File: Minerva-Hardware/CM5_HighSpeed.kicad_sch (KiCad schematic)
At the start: 13 parts, among them J16 Conn_01x22_Female, J5 Conn_01x22_Female, J6 THD-02-R, U6 AP22653W6

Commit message: Rename and commit actions due to mishap of location naming/saving
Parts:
- added J1: HDMI_D_1.4, Connector_Video:HDMI_A_Kycon_KDMIX-SL1-NS-WS-B15_VerticalRightAngle, symbol Connector:HDMI_D_1.4
- U6: Field5 31-AP22653W6-7CT-ND -> AP2553W6-7DICT-ND
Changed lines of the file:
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@@
 			)
 		)
-		(property "Datasheet" "https://fscdn.rohm.com/en/products/databook/datasheet/passive/resistor/chip_resistor/mcr-e.pdf"
+		(property "Datasheet" "~"
 			(at 207.01 110.49 0)
 			(effects
@@
 			)
 		)
-		(property "Description" ""
+		(property "Description" "Resistor"
 			(at 207.01 110.49 0)
 			(effects
@@
 			)
 		)
-		(property "Datasheet" "https://fscdn.rohm.com/en/products/databook/datasheet/passive/resistor/chip_resistor/mcr-e.pdf"
+		(property "Datasheet" "~"
 			(at 214.63 110.49 0)
 			(effects
@@
 			)
 		)
-		(property "Description" ""
+		(property "Description" "Resistor"
 			(at 214.63 110.49 0)
 			(effects
@@
 			)
 		)
-		(property "Datasheet" "https://www.hirose.com/product/document?clcode=&productname=&series=FH12&documenttype=Catalog&lang=en&documentid=D31648_en"
+		(property "Datasheet" "~"
 			(at 156.21 50.8 0)
 			(effects
@@
 			)
 		)
-		(property "Description" ""
+		(property "Description" "Generic connector, single row, 01x22, script generated"
 			(at 156.21 50.8 0)
 			(effects
@@
 			)
 		)
-		(property "Datasheet" "https://www.hirose.com/product/document?clcode=&productname=&series=FH12&documenttype=Catalog&lang=en&documentid=D31648_en"
+		(property "Datasheet" "~"
 			(at 156.21 121.92 0)
 			(effects
@@
 			)
 		)
-		(property "Description" ""
+		(property "Description" "Generic connector, single row, 01x22, script generated"
 			(at 156.21 121.92 0)
 			(effects
@@
 			)
 		)
-		(property "Datasheet" "https://www.toby.co.uk/uploads/publications/1673.pdf"
+		(property "Datasheet" "~"
 			(at 196.85 119.38 0)
 			(effects
@@
 			)
 		)
-		(property "Description" ""
+		(property "Description" "Generic connector, double row, 02x02, odd/even pin numbering scheme (row 1 odd numbers, row 2 even numbers), script generated (kicad-library-utils/schlib/autogen/connector/)"
 			(at 196.85 119.38 0)
 			(effects
@@
 				(path "/e63e39d7-6ac0-4ffd-8aa3-1841a4541b55/00000000-0000-0000-0000-00005cff70b1"
 					(reference "J6")
+					(unit 1)
+				)
+			)
+		)
+	)
+	(symbol
+		(lib_id "Connector:HDMI_D_1.4")
+		(at 223.52 46.99 0)
+		(unit 1)
+		(exclude_from_sim no)
+		(in_bom yes)
+		(on_board yes)
+		(dnp no)
+		(fields_autoplaced yes)
+		(property "Reference" "J1"
+			(at 234.95 45.7199 0)
+			(effects
+				(font
+					(size 1.27 1.27)
+				)
+				(justify left)
+			)
+		)
+		(property "Value" "HDMI_D_1.4"
+			(at 234.95 48.2599 0)
+			(effects
+				(font
+					(size 1.27 1.27)
+				)
+				(justify left)
+			)
+		)
+		(property "Footprint" "Connector_Video:HDMI_A_Kycon_KDMIX-SL1-NS-WS-B15_VerticalRightAngle"
+			(at 224.155 46.99 0)
+			(effects
+				(font
+					(size 1.27 1.27)
+				)
+				(hide yes)
+			)
+		)
+		(property "Datasheet" "http://pinoutguide.com/PortableDevices/micro_hdmi_type_d_pinout.shtml"
+			(at 224.155 46.99 0)
+			(effects
+				(font
+					(size 1.27 1.27)
+				)
+				(hide yes)
+			)
+		)
+		(property "Description" "HDMI 1.4+ type D connector"
+			(at 223.52 46.99 0)
+			(effects
+				(font
+					(size 1.27 1.27)
+				)
+				(hide yes)
+			)
+		)
+		(pin "12"
+		)
+		(pin "7"
+		)
+		(pin "10"
+		)
+		(pin "19"
+		)
+		(pin "15"
+		)
+		(pin "5"
+		)
+		(pin "18"
+		)
+		(pin "16"
+		)
+		(pin "SH"
+		)
+		(pin "14"
+		)
+		(pin "13"
+		)
+		(pin "1"
+		)
+		(pin "17"
+		)
+		(pin "4"
+		)
+		(pin "2"
+		)
+		(pin "11"
+		)
+		(pin "9"
+		)
+		(pin "6"
+		)
+		(pin "3"
+		)
+		(pin "8"
+		)
+		(instances
+			(project "CM5IO"
+				(path "/e63e39d7-6ac0-4ffd-8aa3-1841a4541b55/00000000-0000-0000-0000-00005cff70b1"
+					(reference "J1")
 					(unit 1)
 				)
@@
 			)
 		)
-		(property "Datasheet" "https://search.murata.co.jp/Ceramy/image/img/A01X/G101/ENG/GRM21BR71A106KA73-01.pdf"
+		(property "Datasheet" "~"
 			(at 100.33 181.61 0)
 			(effects
@@
 			)
 		)
-		(property "Description" ""
+		(property "Description" "Unpolarized capacitor"
 			(at 100.33 181.61 0)
 			(effects
@@
 			)
 		)
-		(property "Datasheet" "https://fscdn.rohm.com/en/products/databook/datasheet/passive/resistor/chip_resistor/mcr-e.pdf"
+		(property "Datasheet" "~"
 			(at 138.43 137.16 0)
 			(effects
@@
 			)
 		)
-		(property "Description" ""
+		(property "Description" "Resistor"
 			(at 138.43 137.16 0)
 			(effects
@@
 			)
 		)
-		(property "Description" ""
+		(property "Description" "Polarized capacitor"
 			(at 87.63 181.61 0)
 			(effects
@@
 			)
 		)
-		(property "Datasheet" "https://fscdn.rohm.com/en/products/databook/datasheet/passive/resistor/chip_resistor/mcr-e.pdf"
+		(property "Datasheet" "~"
 			(at 78.74 177.8 0)
 			(effects
@@
 			)
 		)
-		(property "Description" ""
+		(property "Description" "Resistor"
 			(at 78.74 177.8 0)
 			(effects
@@
 			)
 		)
-		(property "Datasheet" "https://search.murata.co.jp/Ceramy/image/img/A01X/G101/ENG/GRM21BR71A106KA73-01.pdf"
+		(property "Datasheet" "~"
 			(at 110.49 181.61 0)
 			(effects
@@
 			)
 		)
-		(property "Description" ""
+		(property "Description" "Unpolarized capacitor"
 			(at 110.49 181.61 0)
 			(effects
@@
 			)
 		)
-		(property "Field5" "	31-AP22653W6-7CT-ND"
+		(property "Field5" "AP2553W6-7DICT-ND"
 			(at 59.69 177.8 0)
 			(effects
@@
 			)
 		)
-		(property "Datasheet" "https://search.murata.co.jp/Ceramy/image/img/A01X/G101/ENG/GRM21BR71A106KA73-01.pdf"
+		(property "Datasheet" "~"
 			(at 29.21 180.34 0)
 			(effects
@@
 			)
 		)
-		(property "Description" ""
+		(property "Description" "Unpolarized capacitor"
 			(at 29.21 180.34 0)
 			(effects

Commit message: renames
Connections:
- net USBOTG_ID: no longer names the net of Module1.101 (USB_OTG_ID)
- no-connect marks 26 -> 27
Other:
- company: Copyright © 2024 Raspberry Pi Ltd. -> (none)
- title: Compute Module 5 IO Board - CM5 - Highspeed -> Minerva Carrier Board - CM5 - Highspeed
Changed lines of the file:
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@@
 	(paper "A4")
 	(title_block
-		(title "Compute Module 5 IO Board - CM5 - Highspeed")
+		(title "Minerva Carrier Board - CM5 - Highspeed")
+		(date "2026-04-13")
 		(rev "1")
-		(company "Copyright © 2024 Raspberry Pi Ltd.")
-		(comment 1 "www.raspberrypi.com")
 	)
 	(text "Jumpers to be fitted if DPHY1 is used\n"
@@
 	)
 	(no_connect
+		(at 99.06 25.4)
+	)
+	(no_connect
 		(at 67.31 180.34)
 	)
@@
 		)
 	)
-	(wire
-		(pts
-			(xy 105.41 25.4) (xy 99.06 25.4)
-		)
-		(stroke
-			(width 0)
-			(type solid)
-		)
-	)
 	(label "DPHY1_D3_P"
 		(at 21.59 144.78 0)
@@
 		)
 	)
-	(hierarchical_label "USBOTG_ID"
-		(shape input)
-		(at 105.41 25.4 0)
-		(effects
-			(font
-				(size 1.27 1.27)
-			)
-			(justify left)
-		)
-	)

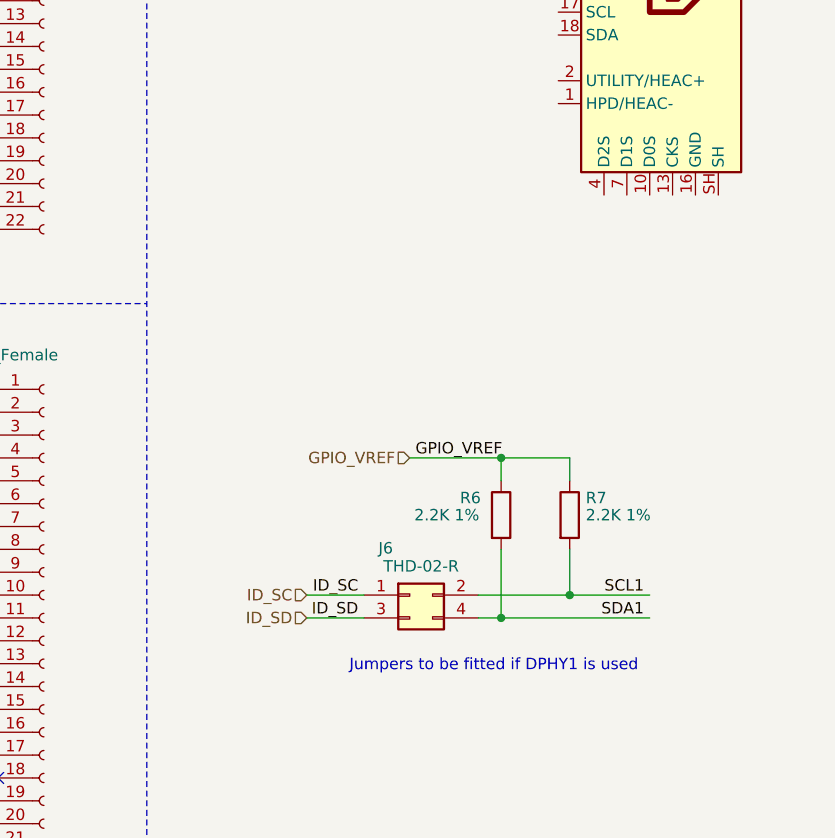
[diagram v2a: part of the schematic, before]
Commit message: Adding MiniPCI-E stuff
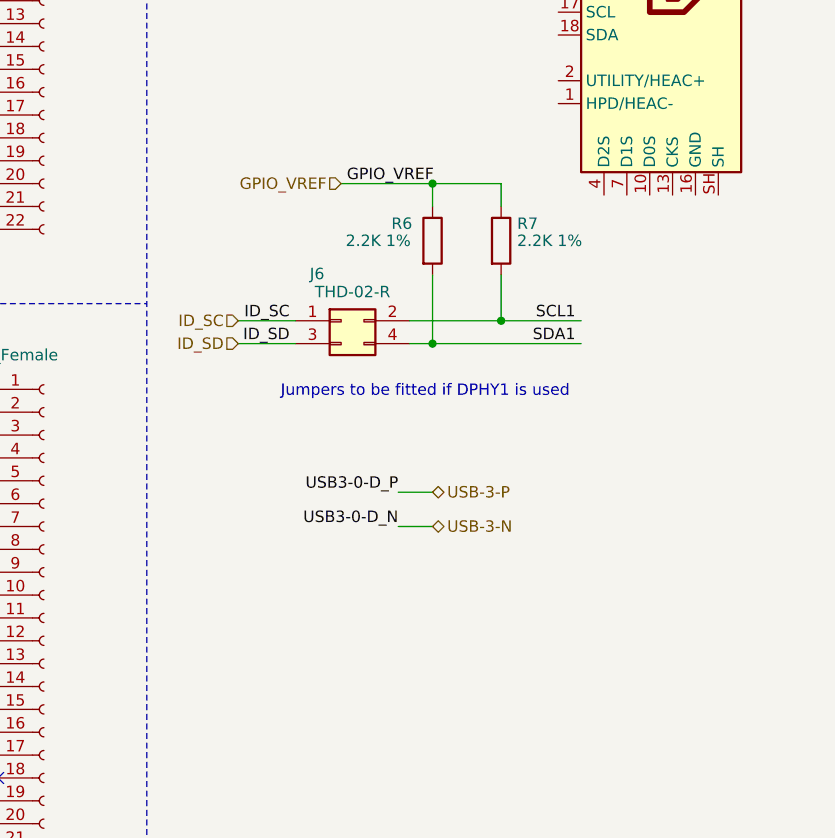
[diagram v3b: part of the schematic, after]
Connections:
- net USB3-0-D_N renamed USB-3-N
- net USB3-0-D_P renamed USB-3-P
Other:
- moved on the sheet: J6, R6, R7

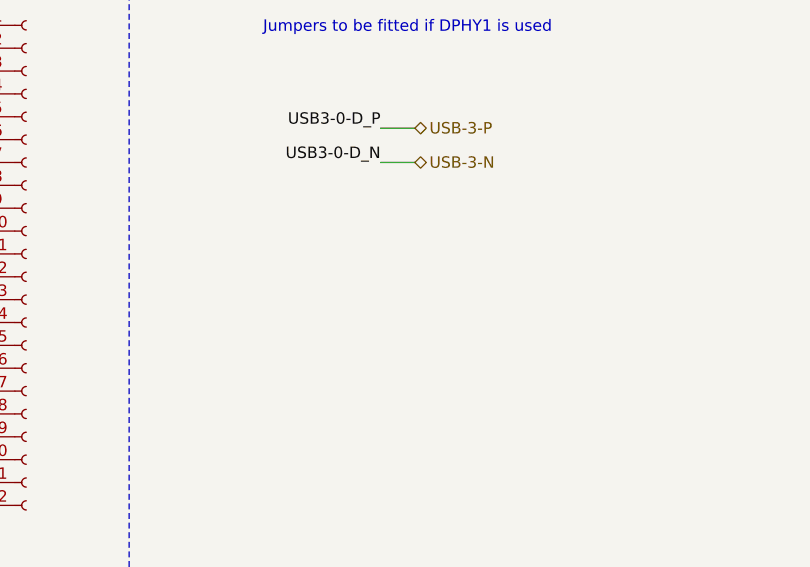
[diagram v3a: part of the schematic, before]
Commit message: Adding in the M.2 B WWAN
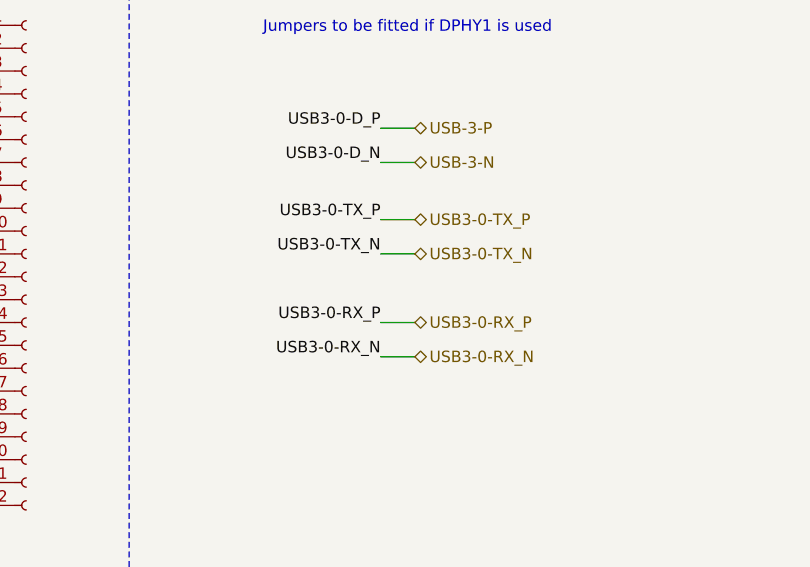
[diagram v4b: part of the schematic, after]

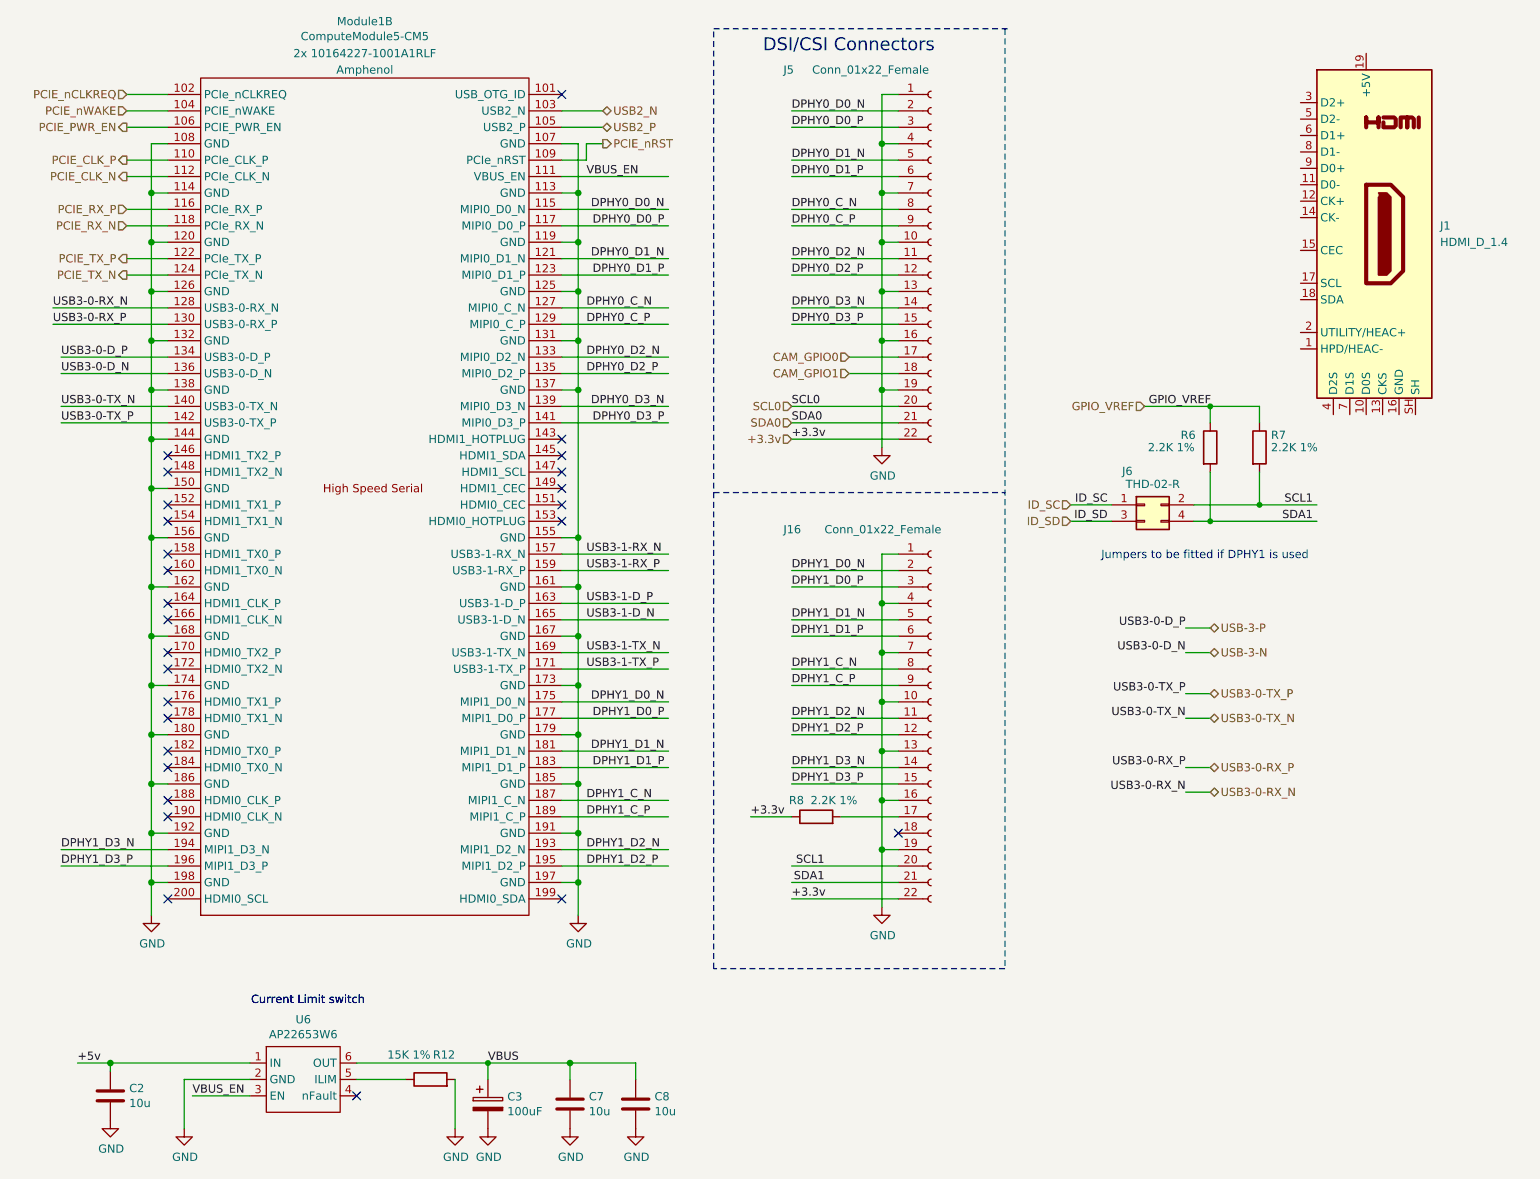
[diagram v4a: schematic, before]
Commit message: Redid the BQ powerpath unit
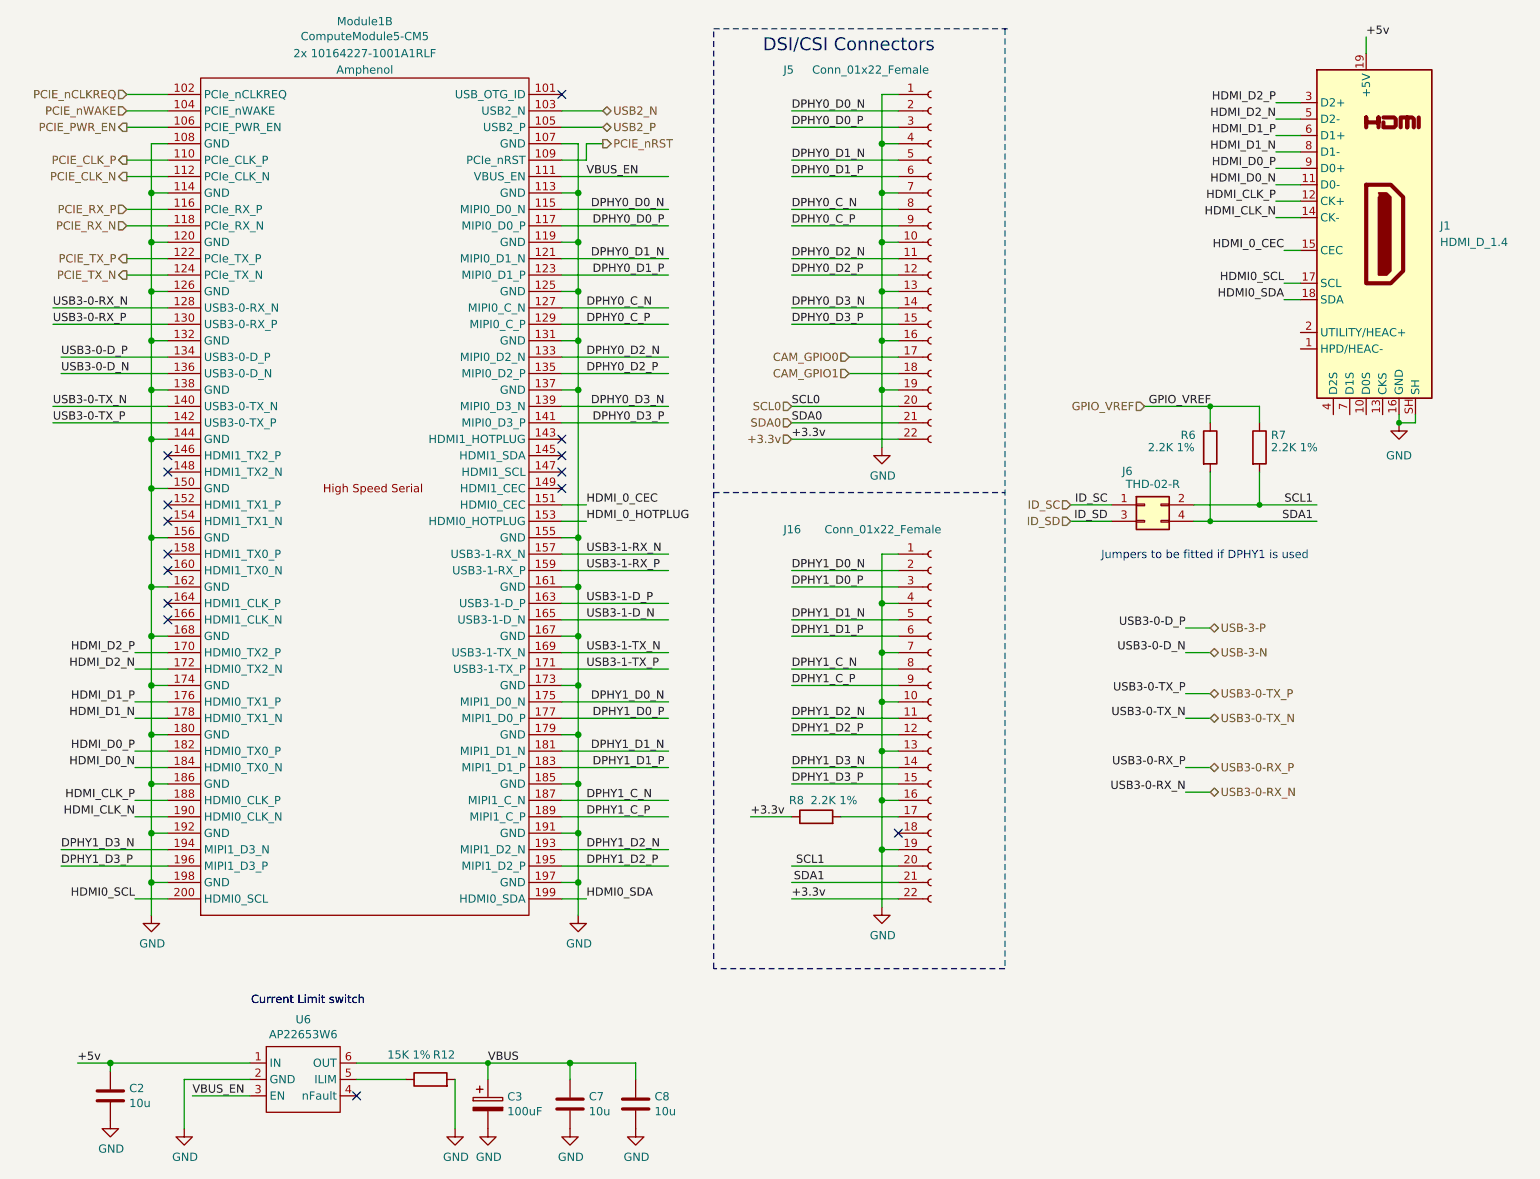
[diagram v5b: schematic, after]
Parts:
- J1: footprint Connector_Video:HDMI_A_Kycon_KDMIX-SL1-NS-WS-B15_VerticalRightAngle -> Connector_FFC-FPC:TE_2-1734839-0_1x20-1MP_P0.5mm_Horizontal
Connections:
- net +5v: now also J1.19 (+5V)
- net GND: now also J1.16 (GND), J1.SH
- net HDMI_0_CEC: now reaches Module1.151 (HDMI0_CEC)
- net HDMI_0_CEC: now also J1.15 (CEC)
- net HDMI_0_HOTPLUG: now reaches Module1.153 (HDMI0_HOTPLUG)
- net HDMI_D2_P: now reaches Module1.170 (HDMI0_TX2_P)
- net HDMI_D2_P: now also J1.3 (D2+)
- net HDMI_D2_N: now reaches Module1.172 (HDMI0_TX2_N)
- net HDMI_D2_N: now also J1.5 (D2-)
- net HDMI_D1_P: now reaches Module1.176 (HDMI0_TX1_P)
- net HDMI_D1_P: now also J1.6 (D1+)
- net HDMI_D1_N: now reaches Module1.178 (HDMI0_TX1_N)
- net HDMI_D1_N: now also J1.8 (D1-)
- net HDMI_D0_P: now reaches Module1.182 (HDMI0_TX0_P)
- net HDMI_D0_P: now also J1.9 (D0+)
- net HDMI_D0_N: now reaches Module1.184 (HDMI0_TX0_N)
- net HDMI_D0_N: now also J1.11 (D0-)
- net HDMI_CLK_P: now reaches Module1.188 (HDMI0_CLK_P)
- net HDMI_CLK_P: now also J1.12 (CK+)
- net HDMI_CLK_N: now reaches Module1.190 (HDMI0_CLK_N)
- net HDMI_CLK_N: now also J1.14 (CK-)
- net HDMI0_SDA: now reaches Module1.199 (HDMI0_SDA)
- net HDMI0_SDA: now also J1.18 (SDA)
- net HDMI0_SCL: now reaches Module1.200 (HDMI0_SCL)
- net HDMI0_SCL: now also J1.17 (SCL)
- no-connect marks 27 -> 15

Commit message: working on pcb more
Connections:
- net USB3-1-D_N is gone; now on net GND: Module1.165 (USB3-1-D_N)
- net USB3-1-D_P is gone; now on net GND: Module1.163 (USB3-1-D_P)
- net USB3-1-RX_N is gone; now on net GND: Module1.157 (USB3-1-RX_N)
- net USB3-1-RX_P is gone; now on net GND: Module1.159 (USB3-1-RX_P)
- net USB3-1-TX_N is gone; now on net GND: Module1.169 (USB3-1-TX_N)
- net USB3-1-TX_P is gone; now on net GND: Module1.171 (USB3-1-TX_P)
- net GND: now also J1.10 (D0S), J1.13 (CKS), J1.4 (D2S), J1.7 (D1S)
- net HDMI_0_HOTPLUG: now also J1.1 (HPD/HEAC-), J1.2 (UTILITY/HEAC+)
- net USB-3-N renamed USB-3_N
- net USB-3-P renamed USB-3_P
- no-connect marks 15 -> 21
